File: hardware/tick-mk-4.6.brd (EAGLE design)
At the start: 96 x 53 mm, 35 parts, among them IC1 ATMEGA328P, IC2 DS1307, IC3 L7805, Y1 16MHz, Y2 32.768kHz

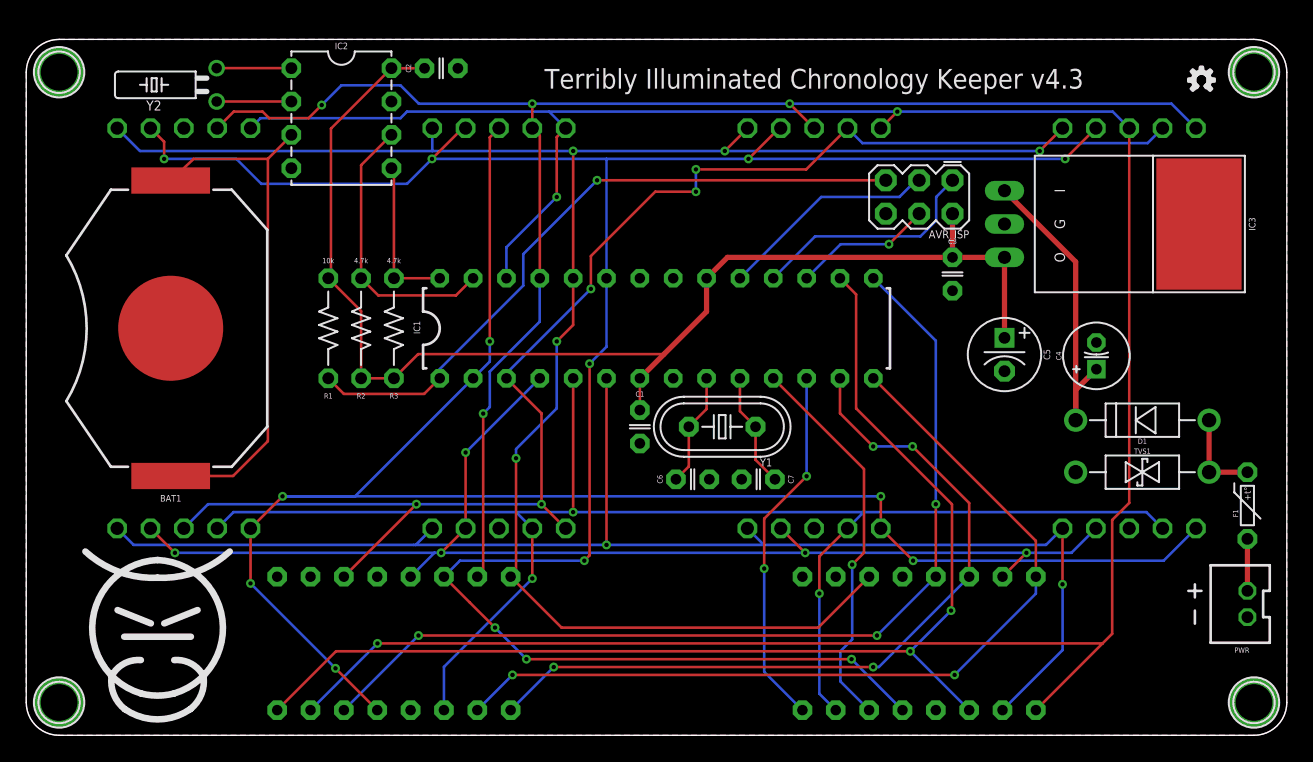
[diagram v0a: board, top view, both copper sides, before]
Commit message: reverting v4.4 and adding 4.6 for compromise between saner layout and all pth/on-hand parts design
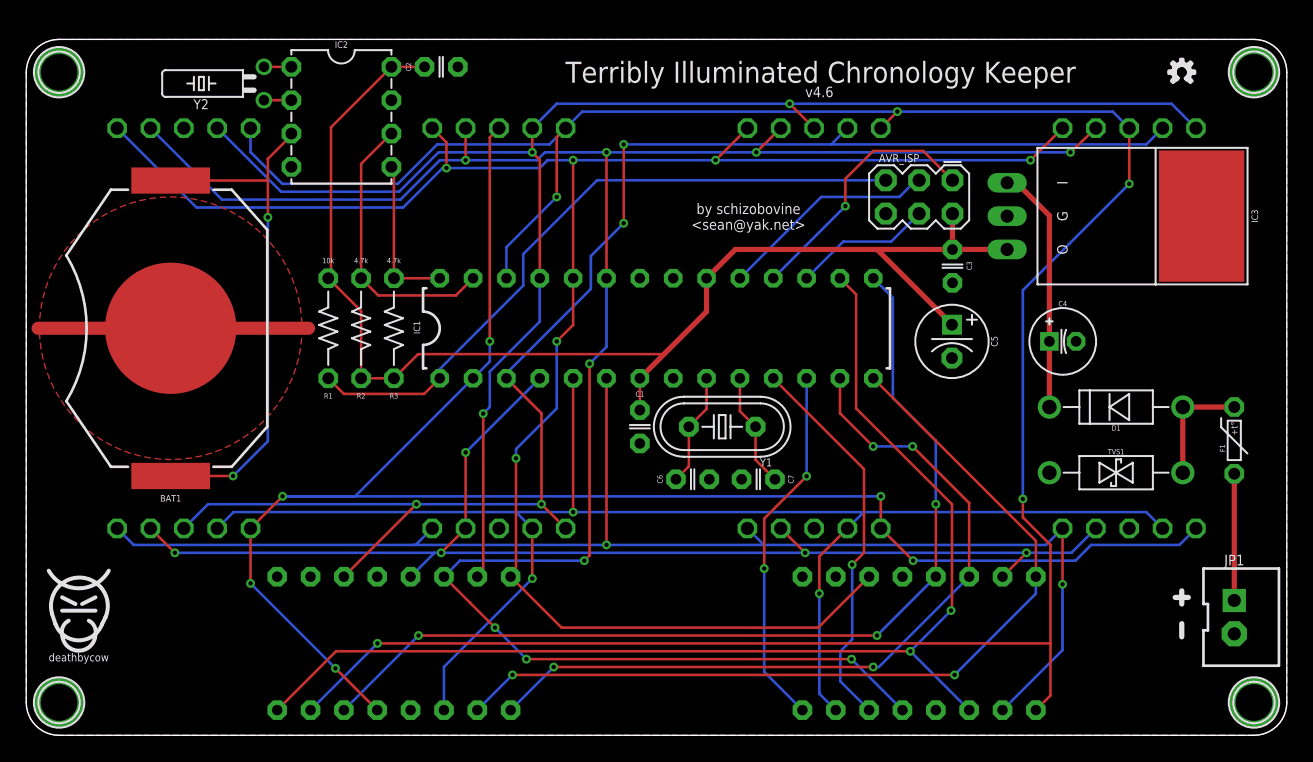
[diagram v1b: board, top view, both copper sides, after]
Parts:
- removed PWR: M02JST-PTH-VERT, A_butts:JST-2-PH-VERT-PTH
- removed U$3: (no value), A_butts:COW
- added JP1: M02JST-XH-VERT, A_butts:JST-2-XH-VERT-PTH
- added U$1: (no value), A_butts:COW_SMALL
- moved F1 5.06 mm to (92.0, 22.5)
- moved C5 4.12 mm to (70.5, 30.0)
- moved Y2 3.60 mm to (18.1, 49.6)
- moved C4 2.79 mm to (78.9, 30.0), turned to 0 degrees
- moved D1 2.24 mm to (83.0, 25.0)
- moved TVS1 2.00 mm to (83.0, 20.0)
- moved U$6 1.62 mm to (88.0, 50.5)
- moved U$7 1.62 mm to (88.0, 50.5)
- moved IC3 0.63 mm to (78.5, 39.5)
- moved C3 0.60 mm to (70.5, 35.7)
- moved C2 0.11 mm to (31.6, 50.9)
- moved IC2 0.10 mm to (24.0, 47.1)
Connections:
- net GND: now also JP1.2; no longer PWR.1
- net N$7: now also JP1.1; no longer PWR.2
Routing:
- net GND: track 0.00 -> 20.6 mm
- net N$7: track 3.96 -> 9.65 mm
- net A1: track 142.5 -> 148.1 mm, vias 5 -> 6
- net N$8: track 24.3 -> 18.8 mm
- net N$3: track 5.69 -> 2.09 mm
- net N$2: track 5.69 -> 2.09 mm
- net D1: track 110.6 -> 113.9 mm, vias 5 -> 4
- net N$4: track 6.88 -> 8.92 mm
- net D12/MISO: track 17.8 -> 19.8 mm, vias 0 -> 1
- net VCC: track 98.1 -> 100.0 mm
- net A0: track 164.9 -> 163.7 mm
- net A3: track 194.5 -> 195.1 mm, vias 3 -> 5
- net N$1: track 40.6 -> 40.1 mm, vias 0 -> 2
- net A2: track 118.5 -> 118.3 mm, vias 4 -> 3
- net D11/MOSI: vias 1 -> 0
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- added copper zone on layer 1, net N$5
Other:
- board text added: "Terribly Illuminated Chronology Keeper"
- board text added: "by schizobovine <sean@yak.net>"
- board text added: "v4.6"
- board text removed: "Terribly Illuminated Chronology Keeper v4.3"

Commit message: i unno
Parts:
- added U$2, U$3: (no value), A_butts:CC-BY-SA-4.0-NO-URL
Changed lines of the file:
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@@
 <attribute name="NAME" x="92" y="12.94" size="0.8128" layer="25" font="vector" ratio="12" align="bottom-center"/>
 </element>
+<element name="U$2" library="A_butts" package="CC-BY-SA-4.0-NO-URL" value="" x="24" y="50" rot="MR0"/>
+<element name="U$3" library="A_butts" package="CC-BY-SA-4.0-NO-URL" value="" x="13.3" y="2.3"/>
 </elements>
 <signals>

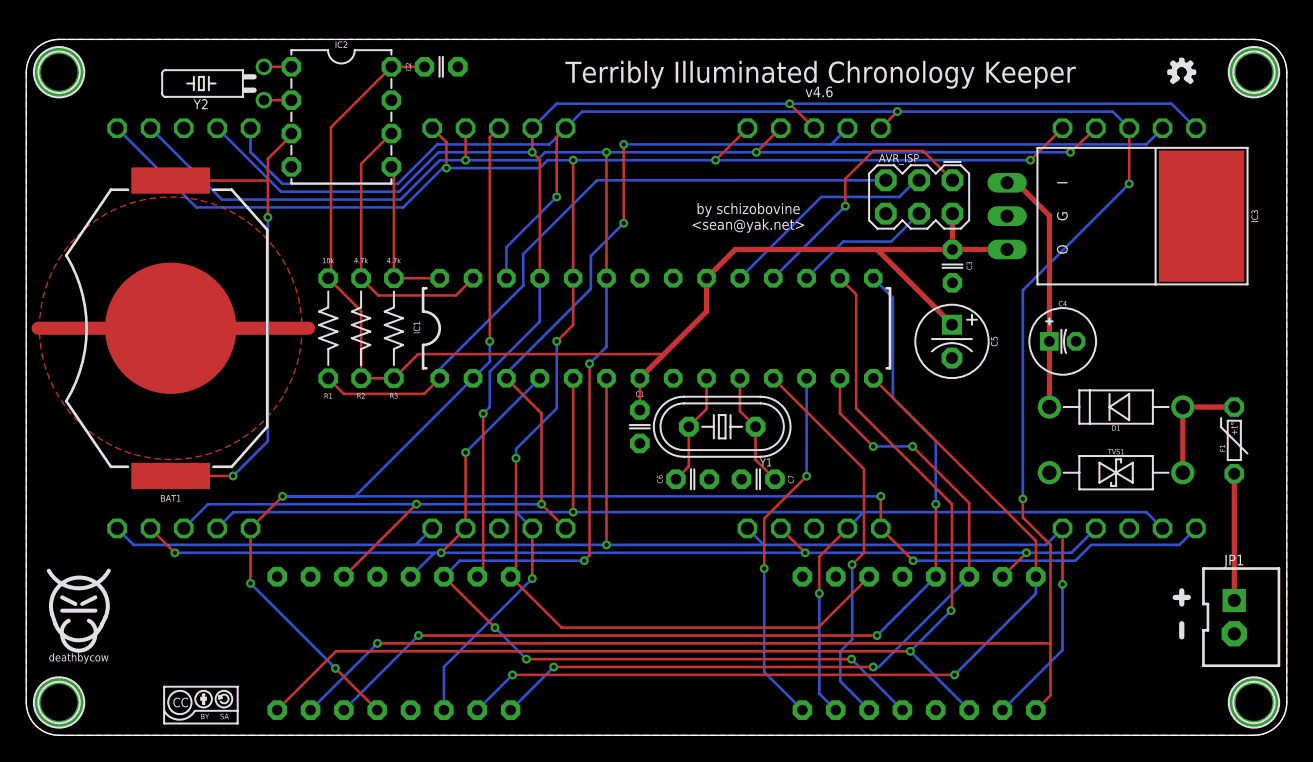
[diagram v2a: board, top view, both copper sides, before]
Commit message: twiddled with dimensions to fit a hammond 1591XXC enclosure
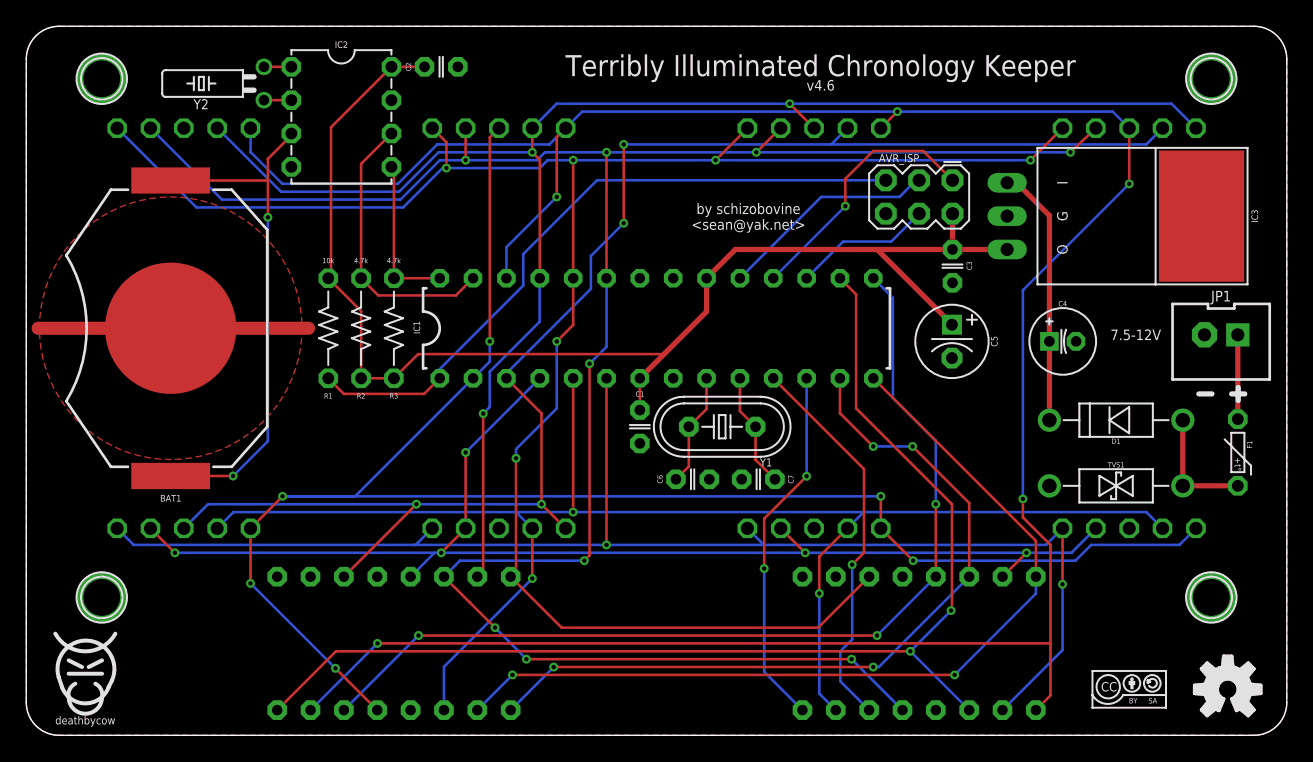
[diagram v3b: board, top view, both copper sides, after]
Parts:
- removed U$6, U$7: (no value), A_butts:OSHWLOGO_MINI
- added U$5, U$8: (no value), A_butts:OSHWLOGO_TOP_0.2
- moved U$3 70.7 mm to (84.0, 3.50)
- moved JP1 21.5 mm to (91.0, 30.5), turned to 180 degrees
- moved H1 8.63 mm to (5.75, 10.5)
- moved H3 8.63 mm to (90.2, 10.5)
- moved U$1 4.83 mm to (4.50, 5.20)
- moved U$4 4.83 mm to (4.50, 5.20)
- moved H2 3.29 mm to (5.75, 50.0)
- moved H4 3.29 mm to (90.2, 50.0)
- moved D1 1.00 mm to (83.0, 24.0)
- moved TVS1 1.00 mm to (83.0, 19.0)
- moved U$2 1.00 mm to (24.0, 51.0)
- moved F1 0.96 mm to (92.3, 21.5), turned to 270 degrees
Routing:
- net N$7: track 9.65 -> 6.42 mm
- net N$8: track 18.8 -> 19.8 mm
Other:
- board size 96 x 53 mm -> 96 x 54 mm
- board text added: "7.5-12V"
